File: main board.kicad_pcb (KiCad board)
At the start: 2 copper layers, 159 x 146 mm, 90 parts, among them J1 #15, J10 #11, J11 #14, J12 #37, J13 #3, J14 #23, J15 #33, J16 #38, J17 #4, J18 #13, J19 #9, J2 Red-Blk, J20 #18, J21 #22, J22 #21, J23 #25, J24 #8, J25 #16, J26 #12, J27 #35, J28 #7, J29 #19, J3 #2, J30 #26, J31 #5, J32 #28, J33 #32, J34 #39, J35 #27, J36 #40, J37 #17, J38 #20, J39 #24, J4 Blk, J40 #29, J41 #30, J42 #31, J43 #34, J44 #36, J45 #Brn, J46 #Blu, J47 #L2, J48 #L1, J5 #1, J6 #6, J7 #10, J8 Red-Yel, J9 Red-Grn, U1 6AL5, U2 ECC83

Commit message: Add earth grounding as in original
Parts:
- removed ? (x4): , 
- removed REF**: OSHW-Logo2_9.8x8mm_Copper, Symbol:OSHW-Logo2_9.8x8mm_Copper
- removed REF**: KiCad-Logo2_8mm_Copper, Symbol:KiCad-Logo2_8mm_Copper
- added H1: MountingHole_Pad, MountingHole:MountingHole_4.3mm_M4_Pad_Via, F.Cu at (105.3, 74.8)
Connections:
- net GNDREF renamed Earth
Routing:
- net Earth: track 8.37 -> 97.0 mm
- added copper zone on B.Cu, net Earth
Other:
- outline, holes or cut-outs redrawn

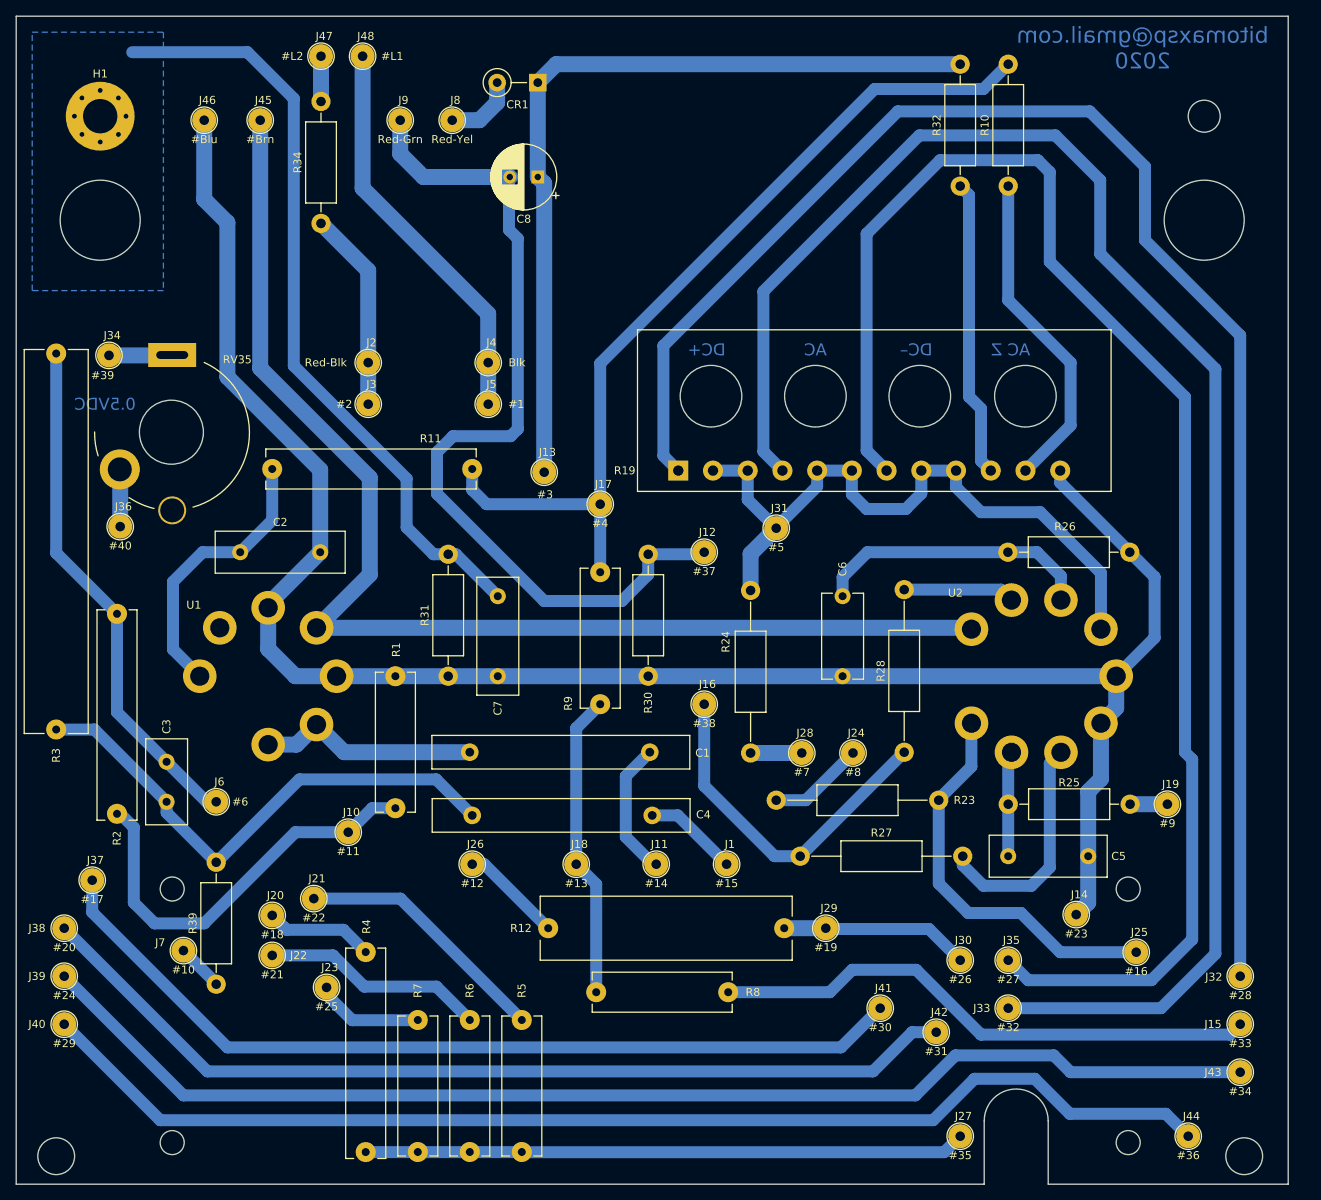
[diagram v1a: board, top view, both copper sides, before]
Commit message: Add D point and remove J references from wire points
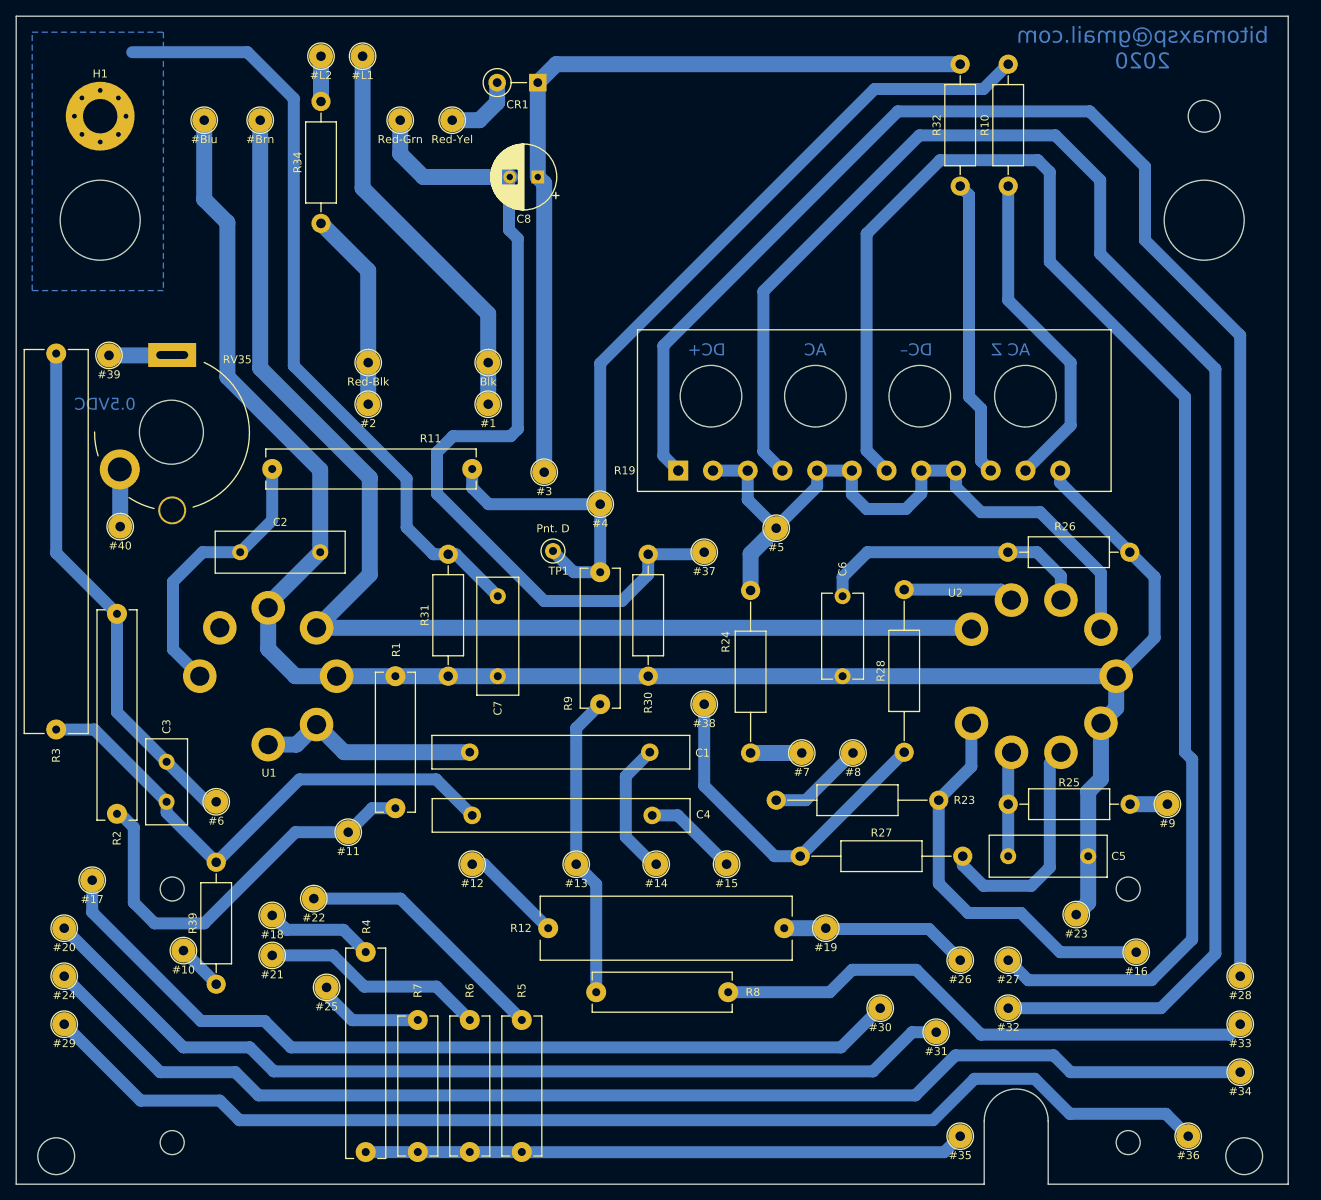
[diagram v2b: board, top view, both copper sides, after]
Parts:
- added TP1: Pnt. D, TestPoint:TestPoint_Loop_D1.80mm_Drill1.0mm_Beaded, F.Cu at (161.9, 129.2)
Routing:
- net Net-(J17-Pad1): track 111.9 -> 118.8 mm
